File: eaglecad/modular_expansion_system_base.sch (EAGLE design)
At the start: 40 parts, among them IC1 74LS244N, IC10 74LS30N, IC2 74LS244N, IC3 74LS244N, IC4 SRAM, IC5 74LS30N, IC6 LM2596T-5.0, IC8 74LS00N, IC9 7805T, J1-INTERRUPTS INTERRUPTS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

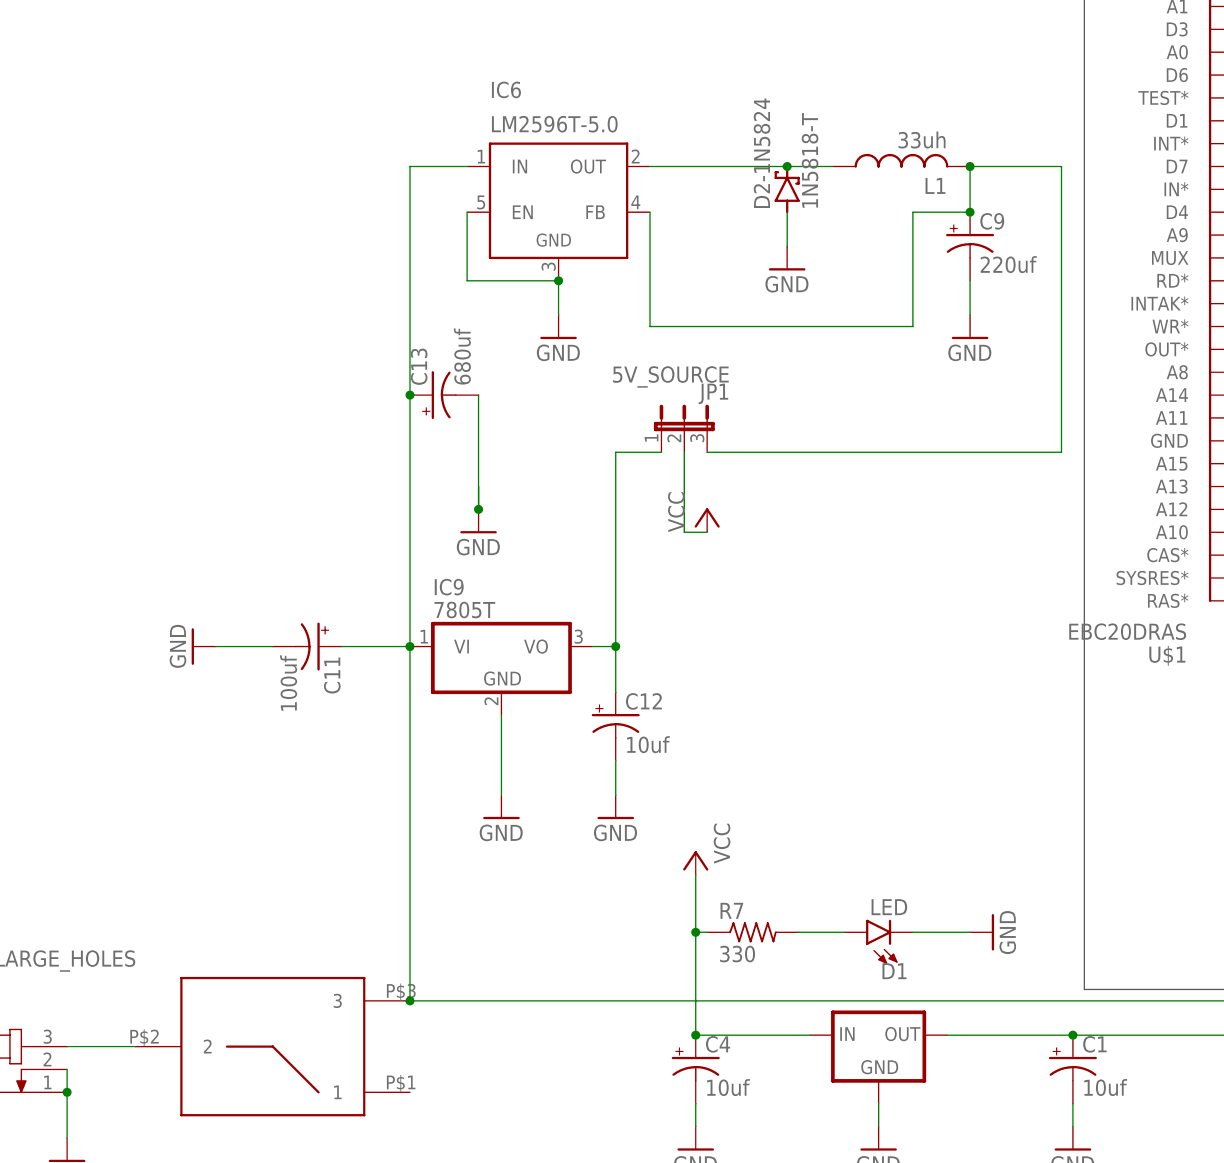
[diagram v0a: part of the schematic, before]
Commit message: Fixes for mount, stand alond joystick boards, level shifters Adafruit
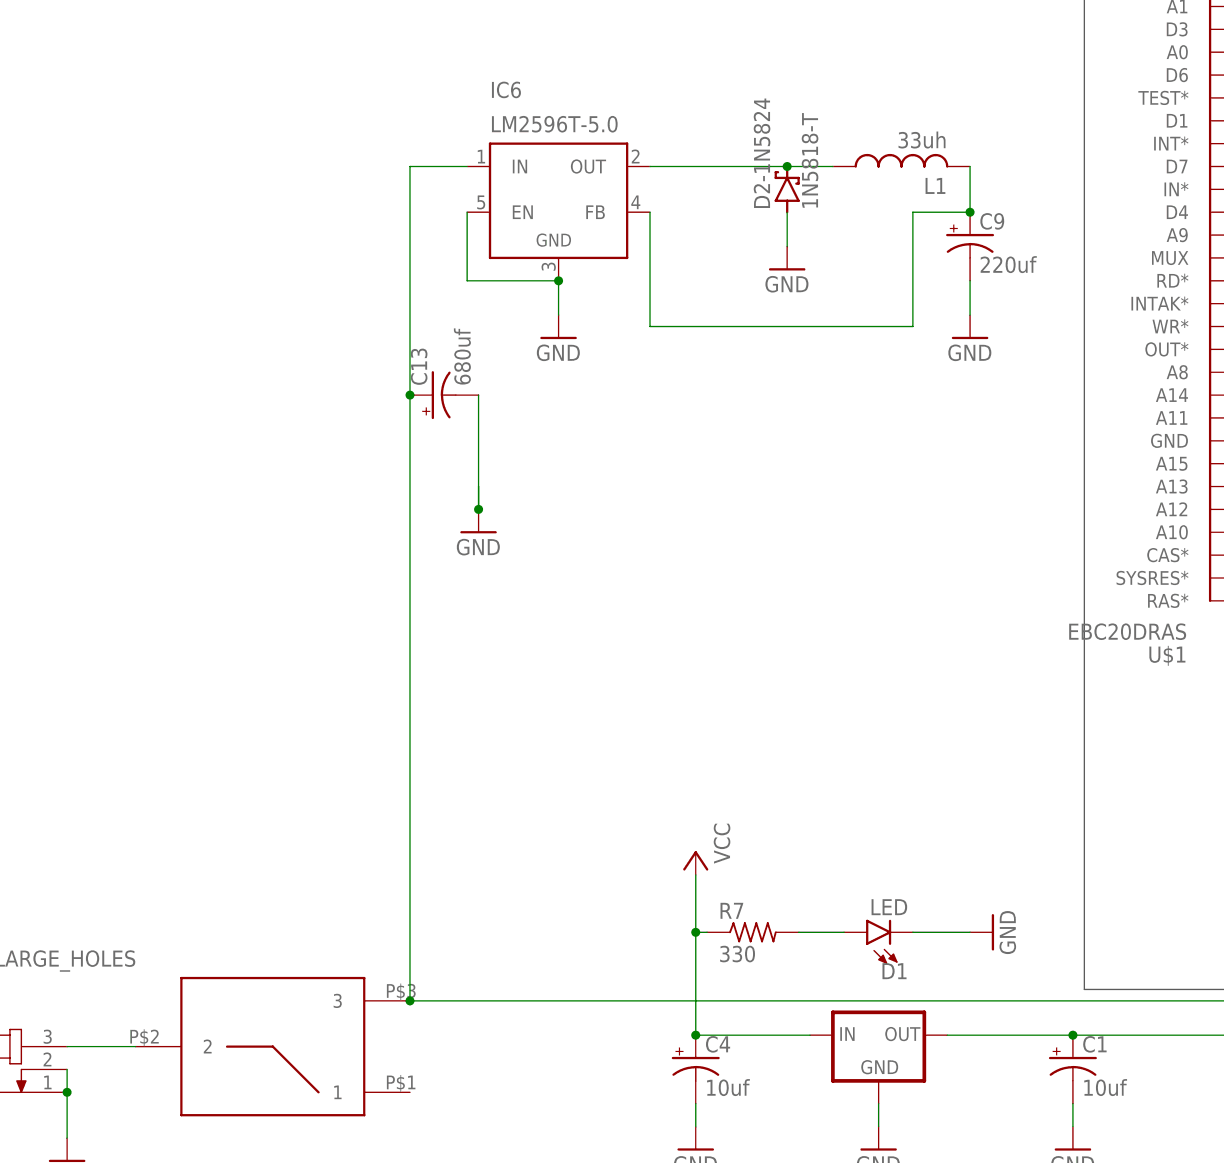
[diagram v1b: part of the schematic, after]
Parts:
- removed C11: 100uf, rcl:CPOL-USE2.5-5
- removed C12: 10uf, resistor:CPOL-USE2.5-5
- removed IC9: 7805T, linear:7805T
- removed JP1: 5V_SOURCE, jumper:JP2E
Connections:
- removed net 5V_FROM_LINEAR_REG: C12.+, IC9.VO, JP1.1
- net 5V_FROM_SWITCHER: no longer JP1.3
- net 9V-POST-SW: no longer C11.+, IC9.VI
- net GND: no longer C11.-, C12.-, IC9.GND
- net VCC: no longer JP1.2
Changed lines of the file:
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@@
 <part name="GND20" library="supply1" library_urn="urn:adsk.eagle:library:371" deviceset="GND" device=""/>
 <part name="SW1" library="TMS99" deviceset="100SP3T1B1M6QE" device=""/>
-<part name="IC9" library="linear" library_urn="urn:adsk.eagle:library:262" deviceset="78*" device="T" package3d_urn="urn:adsk.eagle:package:16414/1" technology="05"/>
-<part name="GND21" library="supply1" library_urn="urn:adsk.eagle:library:371" deviceset="GND" device=""/>
-<part name="C11" library="rcl" library_urn="urn:adsk.eagle:library:334" deviceset="CPOL-US" device="E2.5-5" package3d_urn="urn:adsk.eagle:package:23344/1" value="100uf"/>
-<part name="GND22" library="supply1" library_urn="urn:adsk.eagle:library:371" deviceset="GND" device=""/>
-<part name="C12" library="resistor" library_urn="urn:adsk.eagle:library:348" deviceset="CPOL-US" device="E2.5-5" package3d_urn="urn:adsk.eagle:package:23344/1" value="10uf"/>
-<part name="GND23" library="supply1" library_urn="urn:adsk.eagle:library:371" deviceset="GND" device=""/>
 <part name="J1-INTERRUPTS" library="SparkFun-Connectors" library_urn="urn:adsk.eagle:library:513" deviceset="CONN_04X2" device="" package3d_urn="urn:adsk.eagle:package:38103/1" value="INTERRUPTS"/>
 <part name="P+1" library="supply1" library_urn="urn:adsk.eagle:library:371" deviceset="VCC" device=""/>
@@
 <part name="C9" library="rcl" library_urn="urn:adsk.eagle:library:334" deviceset="CPOL-US" device="E2.5-5" package3d_urn="urn:adsk.eagle:package:23344/1" value="220uf"/>
 <part name="GND25" library="supply1" library_urn="urn:adsk.eagle:library:371" deviceset="GND" device=""/>
-<part name="JP1" library="jumper" library_urn="urn:adsk.eagle:library:252" deviceset="JP2E" device="" package3d_urn="urn:adsk.eagle:package:15452/1" value="5V_SOURCE"/>
-<part name="P+7" library="supply1" library_urn="urn:adsk.eagle:library:371" deviceset="VCC" device=""/>
 <part name="C13" library="rcl" library_urn="urn:adsk.eagle:library:334" deviceset="CPOL-US" device="E3.5-8" package3d_urn="urn:adsk.eagle:package:23360/2" value="680uf"/>
 </parts>
@@
 </instance>
 <instance part="SW1" gate="G$1" x="40.64" y="26.67" smashed="yes" rot="R180"/>
-<instance part="IC9" gate="A1" x="55.88" y="60.96" smashed="yes">
-<attribute name="NAME" x="48.26" y="66.675" size="1.778" layer="95"/>
-<attribute name="VALUE" x="48.26" y="64.135" size="1.778" layer="96"/>
-</instance>
-<instance part="GND21" gate="1" x="55.88" y="41.91" smashed="yes">
-<attribute name="VALUE" x="53.34" y="39.37" size="1.778" layer="96"/>
-</instance>
-<instance part="C11" gate="G$1" x="35.56" y="60.96" smashed="yes" rot="R270">
-<attribute name="NAME" x="36.195" y="59.944" size="1.778" layer="95" rot="R270"/>
-<attribute name="VALUE" x="31.369" y="59.944" size="1.778" layer="96" rot="R270"/>
-</instance>
-<instance part="GND22" gate="1" x="21.59" y="60.96" smashed="yes" rot="R270">
-<attribute name="VALUE" x="19.05" y="63.5" size="1.778" layer="96" rot="R270"/>
-</instance>
-<instance part="C12" gate="G$1" x="68.58" y="53.34" smashed="yes">
-<attribute name="NAME" x="69.596" y="53.975" size="1.778" layer="95"/>
-<attribute name="VALUE" x="69.596" y="49.149" size="1.778" layer="96"/>
-</instance>
-<instance part="GND23" gate="1" x="68.58" y="41.91" smashed="yes">
-<attribute name="VALUE" x="66.04" y="39.37" size="1.778" layer="96"/>
-</instance>
 <instance part="J1-INTERRUPTS" gate="G$1" x="389.89" y="68.58" smashed="yes">
 <attribute name="VALUE" x="386.08" y="61.214" size="1.778" layer="96" font="vector"/>
@@
 <instance part="GND25" gate="1" x="107.95" y="95.25" smashed="yes">
 <attribute name="VALUE" x="105.41" y="92.71" size="1.778" layer="96"/>
-</instance>
-<instance part="JP1" gate="1" x="76.2" y="85.09" smashed="yes">
-<attribute name="NAME" x="81.28" y="90.17" size="1.778" layer="95" rot="R180"/>
-<attribute name="VALUE" x="81.28" y="92.075" size="1.778" layer="96" rot="R180"/>
-</instance>
-<instance part="P+7" gate="VCC" x="78.74" y="76.2" smashed="yes">
-<attribute name="VALUE" x="76.2" y="73.66" size="1.778" layer="96" rot="R90"/>
 </instance>
 <instance part="C13" gate="G$1" x="48.26" y="88.9" smashed="yes" rot="R90">
@@
 <junction x="135.89" y="205.74"/>
 <pinref part="GND20" gate="1" pin="GND"/>
-</segment>
-<segment>
-<pinref part="IC9" gate="A1" pin="GND"/>
-<pinref part="GND21" gate="1" pin="GND"/>
-<wire x1="55.88" y1="53.34" x2="55.88" y2="44.45" width="0.1524" layer="91"/>
-</segment>
-<segment>
-<pinref part="C11" gate="G$1" pin="-"/>
-<pinref part="GND22" gate="1" pin="GND"/>
-<wire x1="30.48" y1="60.96" x2="24.13" y2="60.96" width="0.1524" layer="91"/>
-</segment>
-<segment>
-<pinref part="C12" gate="G$1" pin="-"/>
-<pinref part="GND23" gate="1" pin="GND"/>
-<wire x1="68.58" y1="48.26" x2="68.58" y2="44.45" width="0.1524" layer="91"/>
 </segment>
 <segment>
@@
 <pinref part="P+6" gate="VCC" pin="VCC"/>
 </segment>
-<segment>
-<pinref part="JP1" gate="1" pin="2"/>
-<wire x1="76.2" y1="82.55" x2="76.2" y2="73.66" width="0.1524" layer="91"/>
-<wire x1="76.2" y1="73.66" x2="78.74" y2="73.66" width="0.1524" layer="91"/>
-<pinref part="P+7" gate="VCC" pin="VCC"/>
-</segment>
 </net>
 <net name="9V-POST-SW" class="0">
 <segment>
 <pinref part="SW1" gate="G$1" pin="3"/>
-<pinref part="IC9" gate="A1" pin="VI"/>
-<wire x1="45.72" y1="60.96" x2="45.72" y2="21.59" width="0.1524" layer="91"/>
-<pinref part="C11" gate="G$1" pin="+"/>
-<wire x1="38.1" y1="60.96" x2="45.72" y2="60.96" width="0.1524" layer="91"/>
-<junction x="45.72" y="60.96"/>
+<wire x1="45.72" y1="88.9" x2="45.72" y2="21.59" width="0.1524" layer="91"/>
 <pinref part="J2_DATA_AND_POWER_CON" gate="G$1" pin="4"/>
 <wire x1="262.89" y1="13.97" x2="262.89" y2="16.51" width="0.1524" layer="91"/>
@@
 <wire x1="52.07" y1="114.3" x2="45.72" y2="114.3" width="0.1524" layer="91"/>
 <wire x1="45.72" y1="114.3" x2="45.72" y2="88.9" width="0.1524" layer="91"/>
-<wire x1="45.72" y1="88.9" x2="45.72" y2="60.96" width="0.1524" layer="91"/>
 <pinref part="C13" gate="G$1" pin="+"/>
 <junction x="45.72" y="88.9"/>
@@
 <pinref part="C9" gate="G$1" pin="+"/>
 <wire x1="107.95" y1="114.3" x2="107.95" y2="109.22" width="0.1524" layer="91"/>
-<junction x="107.95" y="114.3"/>
-<wire x1="107.95" y1="114.3" x2="118.11" y2="114.3" width="0.1524" layer="91"/>
-<pinref part="JP1" gate="1" pin="3"/>
-<wire x1="118.11" y1="114.3" x2="118.11" y2="82.55" width="0.1524" layer="91"/>
-<wire x1="118.11" y1="82.55" x2="78.74" y2="82.55" width="0.1524" layer="91"/>
 <pinref part="IC6" gate="NC1" pin="FB"/>
 <wire x1="101.6" y1="96.52" x2="72.39" y2="96.52" width="0.1524" layer="91"/>
@@
 </segment>
 </net>
-<net name="5V_FROM_LINEAR_REG" class="0">
-<segment>
-<pinref part="IC9" gate="A1" pin="VO"/>
-<wire x1="68.58" y1="60.96" x2="66.04" y2="60.96" width="0.1524" layer="91"/>
-<pinref part="C12" gate="G$1" pin="+"/>
-<wire x1="68.58" y1="55.88" x2="68.58" y2="60.96" width="0.1524" layer="91"/>
-<pinref part="JP1" gate="1" pin="1"/>
-<wire x1="73.66" y1="82.55" x2="68.58" y2="82.55" width="0.1524" layer="91"/>
-<wire x1="68.58" y1="82.55" x2="68.58" y2="60.96" width="0.1524" layer="91"/>
-<junction x="68.58" y="60.96"/>
-</segment>
-</net>
